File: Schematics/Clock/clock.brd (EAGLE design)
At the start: 53.3 x 50.3 mm, 13 parts, among them IC1 NE555N

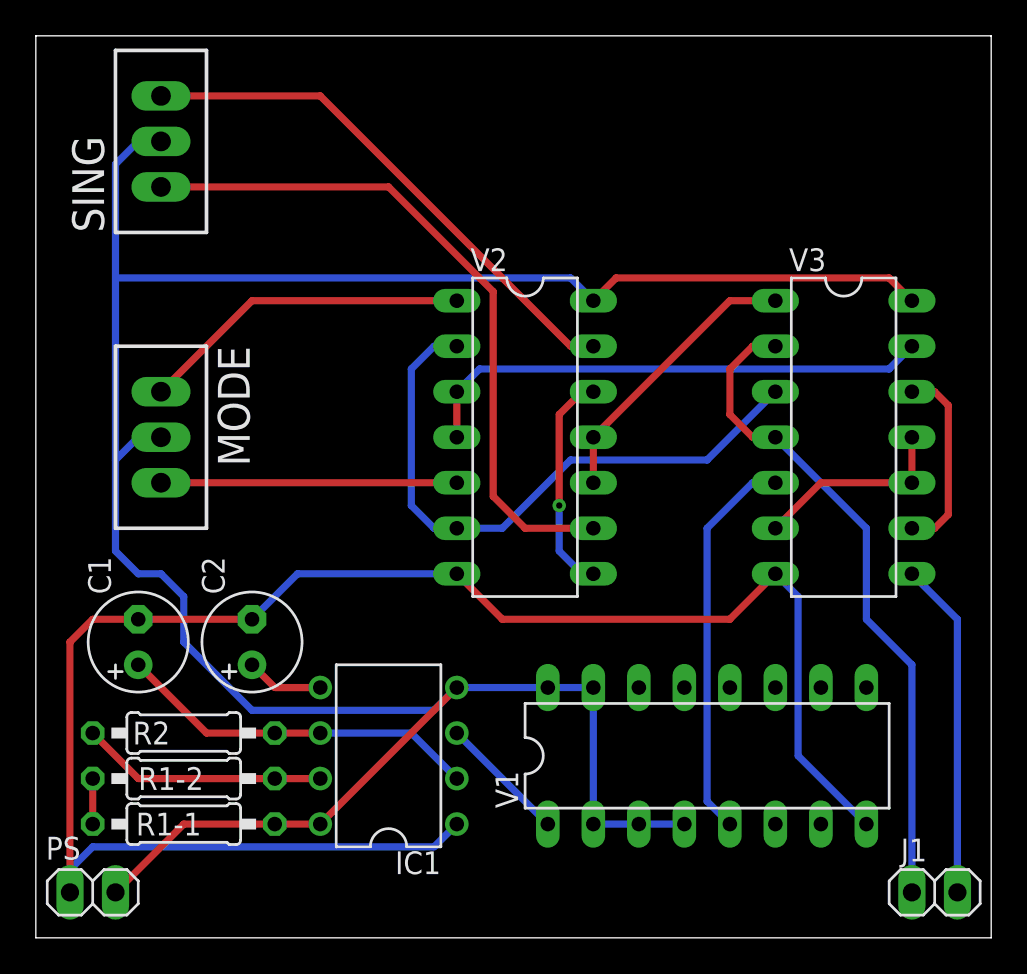
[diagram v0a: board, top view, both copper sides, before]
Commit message: Added pull down resisotors to NAND gates. Maybe 'single' will be button.
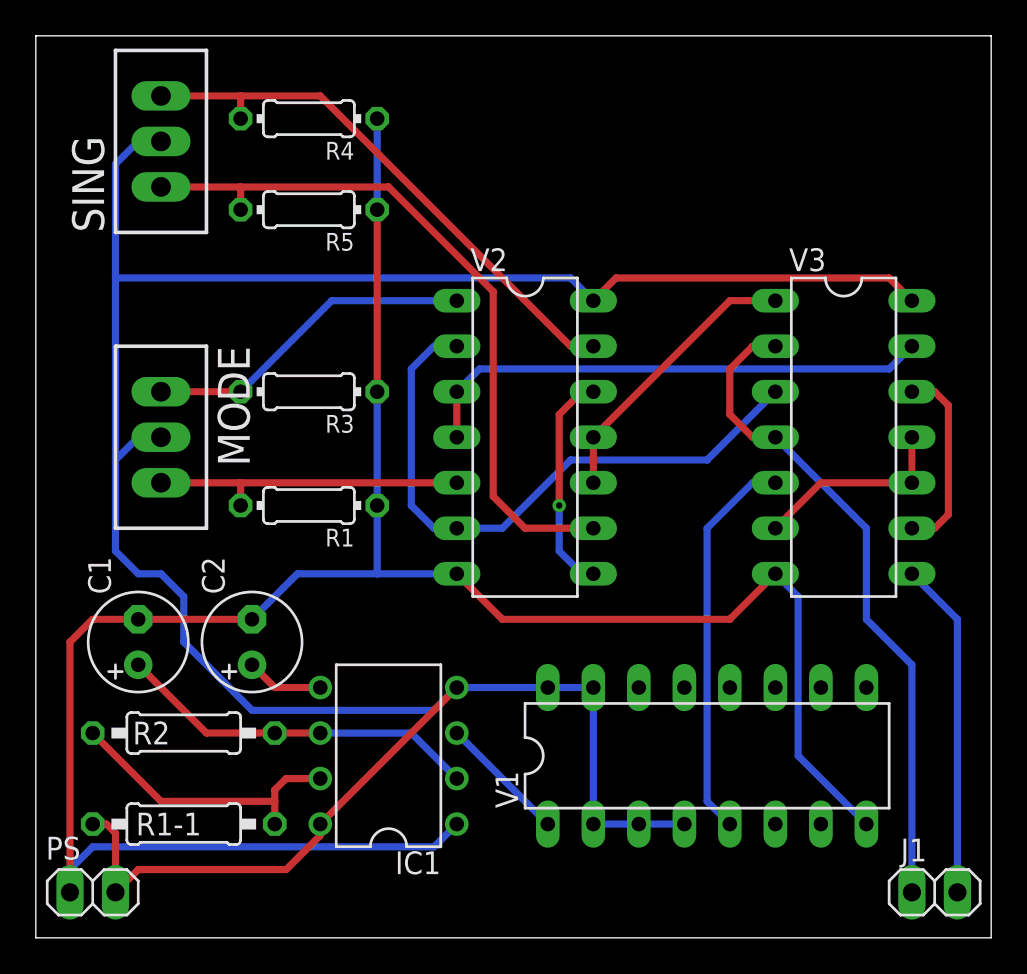
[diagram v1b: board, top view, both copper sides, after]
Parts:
- removed R1-2: (no value), rcl:0207/10
- added R1, R3, R4, R5: (no value), rcl:0204/7
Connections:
- removed net N$4: R1-1.1, R1-2.1
- net GND: now also R1.1, R3.1, R4.1, R5.1
- net N$11: now also R5.2
- net N$12: now also R4.2
- net N$2: now also R1-1.2; no longer R1-2.2
- net N$7: now also R3.2
- net N$8: now also R1.2
- net VCC: now also R1-1.1; no longer R1-1.2
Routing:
- net GND: track 97.0 -> 122.4 mm
- net VCC: track 142.6 -> 147.8 mm
- net N$2: track 13.8 -> 16.4 mm
- net N$4: track 2.54 -> 0.00 mm
- net N$12: track 29.9 -> 31.2 mm
- net N$8: track 16.5 -> 17.8 mm
- net N$11: track 38.7 -> 40.0 mm
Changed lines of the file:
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@@
 <attribute name="VALUE" x="5.9944" y="5.715" size="1.27" layer="27" ratio="10"/>
-</element>
-<element name="R1-2" library="rcl" library_urn="urn:adsk.eagle:library:334" package="0207/10" package3d_urn="urn:adsk.eagle:package:23491/2" value="" x="8.255" y="8.89" smashed="yes">
-<attribute name="NAME" x="5.715" y="8.255" size="1.27" layer="25" ratio="10"/>
-<attribute name="POPULARITY" value="81" x="40.005" y="-45.72" size="1.778" layer="27" display="off"/>
-<attribute name="SPICEPREFIX" value="R" x="40.005" y="-45.72" size="1.778" layer="27" display="off"/>
-<attribute name="VALUE" x="5.9944" y="8.255" size="1.27" layer="27" ratio="10"/>
 </element>
 <element name="R2" library="rcl" library_urn="urn:adsk.eagle:library:334" package="0207/10" package3d_urn="urn:adsk.eagle:package:23491/2" value="" x="8.255" y="11.43" smashed="yes" rot="R180">
@@
 <attribute name="POPULARITY" value="0" x="4.445" y="5.08" size="1.778" layer="27" rot="R270" display="off"/>
 <attribute name="VALUE" x="44.45" y="34.671" size="1.27" layer="27" ratio="10" rot="R270"/>
+</element>
+<element name="R1" library="rcl" library_urn="urn:adsk.eagle:library:334" package="0204/7" package3d_urn="urn:adsk.eagle:package:23498/2" value="" x="15.24" y="24.13" smashed="yes" rot="R180">
+<attribute name="NAME" x="17.78" y="22.8346" size="0.9906" layer="25" ratio="10" rot="R180"/>
+<attribute name="POPULARITY" value="79" x="15.24" y="24.13" size="1.778" layer="27" rot="R180" display="off"/>
+<attribute name="SPICEPREFIX" value="R" x="15.24" y="24.13" size="1.778" layer="27" rot="R180" display="off"/>
+<attribute name="VALUE" x="16.8656" y="24.6126" size="0.9906" layer="27" ratio="10" rot="R180"/>
+</element>
+<element name="R3" library="rcl" library_urn="urn:adsk.eagle:library:334" package="0204/7" package3d_urn="urn:adsk.eagle:package:23498/2" value="" x="15.24" y="30.48" smashed="yes" rot="R180">
+<attribute name="NAME" x="17.78" y="29.1846" size="0.9906" layer="25" ratio="10" rot="R180"/>
+<attribute name="POPULARITY" value="79" x="15.24" y="30.48" size="1.778" layer="27" rot="R180" display="off"/>
+<attribute name="SPICEPREFIX" value="R" x="15.24" y="30.48" size="1.778" layer="27" rot="R180" display="off"/>
+<attribute name="VALUE" x="16.8656" y="30.9626" size="0.9906" layer="27" ratio="10" rot="R180"/>
+</element>
+<element name="R4" library="rcl" library_urn="urn:adsk.eagle:library:334" package="0204/7" package3d_urn="urn:adsk.eagle:package:23498/2" value="" x="15.24" y="45.72" smashed="yes" rot="R180">
+<attribute name="NAME" x="17.78" y="44.4246" size="0.9906" layer="25" ratio="10" rot="R180"/>
+<attribute name="POPULARITY" value="79" x="15.24" y="45.72" size="1.778" layer="27" rot="R180" display="off"/>
+<attribute name="SPICEPREFIX" value="R" x="15.24" y="45.72" size="1.778" layer="27" rot="R180" display="off"/>
+<attribute name="VALUE" x="16.8656" y="46.2026" size="0.9906" layer="27" ratio="10" rot="R180"/>
+</element>
+<element name="R5" library="rcl" library_urn="urn:adsk.eagle:library:334" package="0204/7" package3d_urn="urn:adsk.eagle:package:23498/2" value="" x="15.24" y="40.64" smashed="yes" rot="R180">
+<attribute name="NAME" x="17.78" y="39.3446" size="0.9906" layer="25" ratio="10" rot="R180"/>
+<attribute name="POPULARITY" value="79" x="15.24" y="40.64" size="1.778" layer="27" rot="R180" display="off"/>
+<attribute name="SPICEPREFIX" value="R" x="15.24" y="40.64" size="1.778" layer="27" rot="R180" display="off"/>
+<attribute name="VALUE" x="16.8656" y="41.1226" size="0.9906" layer="27" ratio="10" rot="R180"/>
 </element>
 </elements>
@@
 <contactref element="R2" pad="2"/>
 <contactref element="IC1" pad="7"/>
-<contactref element="R1-2" pad="2"/>
-<wire x1="13.335" y1="8.89" x2="5.715" y2="8.89" width="0.4" layer="1"/>
-<wire x1="5.715" y1="8.89" x2="3.175" y2="11.43" width="0.4" layer="1"/>
-<wire x1="13.335" y1="8.89" x2="15.875" y2="8.89" width="0.4" layer="1"/>
+<contactref element="R1-1" pad="2"/>
+<wire x1="13.335" y1="6.35" x2="13.335" y2="7.62" width="0.4" layer="1"/>
+<wire x1="13.335" y1="7.62" x2="13.335" y2="8.255" width="0.4" layer="1"/>
+<wire x1="13.335" y1="8.255" x2="13.97" y2="8.89" width="0.4" layer="1"/>
+<wire x1="13.97" y1="8.89" x2="15.875" y2="8.89" width="0.4" layer="1"/>
+<wire x1="3.175" y1="11.43" x2="6.985" y2="7.62" width="0.4" layer="1"/>
+<wire x1="6.985" y1="7.62" x2="13.335" y2="7.62" width="0.4" layer="1"/>
 </signal>
 <signal name="N$3">
@@
 <contactref element="IC1" pad="8"/>
 <contactref element="IC1" pad="4"/>
-<contactref element="R1-1" pad="2"/>
 <contactref element="V1" pad="4"/>
 <contactref element="V1" pad="2"/>
@@
 <contactref element="V3" pad="14"/>
 <contactref element="V1" pad="16"/>
-<wire x1="13.335" y1="6.35" x2="15.875" y2="6.35" width="0.4" layer="1"/>
-<wire x1="4.445" y1="2.54" x2="8.255" y2="6.35" width="0.4" layer="1"/>
-<wire x1="8.255" y1="6.35" x2="13.335" y2="6.35" width="0.4" layer="1"/>
 <wire x1="15.875" y1="6.35" x2="23.495" y2="13.97" width="0.4" layer="1"/>
 <wire x1="31.115" y1="13.97" x2="31.115" y2="6.35" width="0.4" layer="16"/>
@@
 <wire x1="31.115" y1="35.56" x2="29.845" y2="36.83" width="0.4" layer="16"/>
 <wire x1="29.845" y1="36.83" x2="4.445" y2="36.83" width="0.4" layer="16"/>
+<contactref element="R1-1" pad="1"/>
+<wire x1="4.445" y1="2.54" x2="4.445" y2="5.842" width="0.4" layer="1"/>
+<wire x1="4.445" y1="5.842" x2="3.937" y2="6.35" width="0.4" layer="1"/>
+<wire x1="3.937" y1="6.35" x2="3.175" y2="6.35" width="0.4" layer="1"/>
+<wire x1="4.445" y1="2.54" x2="5.715" y2="3.81" width="0.4" layer="1"/>
+<wire x1="5.715" y1="3.81" x2="13.97" y2="3.81" width="0.4" layer="1"/>
+<wire x1="13.97" y1="3.81" x2="15.875" y2="5.715" width="0.4" layer="1"/>
+<wire x1="15.875" y1="5.715" x2="15.875" y2="6.35" width="0.4" layer="1"/>
 </signal>
 <signal name="GND">
@@
 <wire x1="42.545" y1="10.16" x2="42.545" y2="19.05" width="0.4" layer="16"/>
 <wire x1="12.065" y1="17.78" x2="14.605" y2="20.32" width="0.4" layer="16"/>
-<wire x1="14.605" y1="20.32" x2="23.495" y2="20.32" width="0.4" layer="16"/>
+<wire x1="14.605" y1="20.32" x2="19.05" y2="20.32" width="0.4" layer="16"/>
+<wire x1="19.05" y1="20.32" x2="23.495" y2="20.32" width="0.4" layer="16"/>
 <wire x1="41.275" y1="20.32" x2="38.735" y2="17.78" width="0.4" layer="1"/>
 <wire x1="26.035" y1="17.78" x2="23.495" y2="20.32" width="0.4" layer="1"/>
 <wire x1="38.735" y1="17.78" x2="26.035" y2="17.78" width="0.4" layer="1"/>
+<contactref element="R1" pad="1"/>
+<contactref element="R3" pad="1"/>
+<contactref element="R4" pad="1"/>
+<contactref element="R5" pad="1"/>
+<wire x1="19.05" y1="24.13" x2="19.05" y2="20.32" width="0.4" layer="16"/>
+<wire x1="19.05" y1="24.13" x2="19.05" y2="30.48" width="0.4" layer="16"/>
+<wire x1="19.05" y1="40.64" x2="19.05" y2="45.72" width="0.4" layer="16"/>
+<wire x1="19.05" y1="40.64" x2="19.05" y2="30.48" width="0.4" layer="1"/>
 </signal>
 <signal name="CLK-0">
@@
 <contactref element="V1" pad="1"/>
 <wire x1="23.495" y1="11.43" x2="28.575" y2="6.35" width="0.4" layer="16"/>
-</signal>
-<signal name="N$4">
-<contactref element="R1-2" pad="1"/>
-<contactref element="R1-1" pad="1"/>
-<wire x1="3.175" y1="6.35" x2="3.175" y2="8.89" width="0.4" layer="1"/>
 </signal>
 <signal name="CLK-1">
@@
 <contactref element="V2" pad="1"/>
 <contactref element="MODE" pad="1"/>
-<wire x1="6.985" y1="30.48" x2="12.065" y2="35.56" width="0.4" layer="1"/>
-<wire x1="12.065" y1="35.56" x2="23.495" y2="35.56" width="0.4" layer="1"/>
+<contactref element="R3" pad="2"/>
+<wire x1="6.985" y1="30.48" x2="11.43" y2="30.48" width="0.4" layer="1"/>
+<wire x1="11.43" y1="30.48" x2="16.51" y2="35.56" width="0.4" layer="16"/>
+<wire x1="16.51" y1="35.56" x2="23.495" y2="35.56" width="0.4" layer="16"/>
 </signal>
 <signal name="N$8">
 <contactref element="V2" pad="5"/>
 <contactref element="MODE" pad="3"/>
-<wire x1="6.985" y1="25.4" x2="23.495" y2="25.4" width="0.4" layer="1"/>
+<wire x1="6.985" y1="25.4" x2="11.43" y2="25.4" width="0.4" layer="1"/>
+<contactref element="R1" pad="2"/>
+<wire x1="11.43" y1="25.4" x2="23.495" y2="25.4" width="0.4" layer="1"/>
+<wire x1="11.43" y1="24.13" x2="11.43" y2="25.4" width="0.4" layer="1"/>
 </signal>
 <signal name="N$11">
 <contactref element="SING" pad="1"/>
 <contactref element="V2" pad="9"/>
-<wire x1="6.985" y1="41.91" x2="19.685" y2="41.91" width="0.4" layer="1"/>
+<wire x1="6.985" y1="41.91" x2="11.43" y2="41.91" width="0.4" layer="1"/>
+<wire x1="11.43" y1="41.91" x2="19.685" y2="41.91" width="0.4" layer="1"/>
 <wire x1="25.527" y1="24.638" x2="27.305" y2="22.86" width="0.4" layer="1"/>
 <wire x1="27.305" y1="22.86" x2="31.115" y2="22.86" width="0.4" layer="1"/>
 <wire x1="19.685" y1="41.91" x2="25.527" y2="36.068" width="0.4" layer="1"/>
 <wire x1="25.527" y1="36.068" x2="25.527" y2="24.638" width="0.4" layer="1"/>
+<contactref element="R5" pad="2"/>
+<wire x1="11.43" y1="40.64" x2="11.43" y2="41.91" width="0.4" layer="1"/>
 </signal>
 <signal name="N$12">
 <contactref element="SING" pad="3"/>
 <contactref element="V2" pad="13"/>
-<wire x1="6.985" y1="46.99" x2="15.875" y2="46.99" width="0.4" layer="1"/>
+<wire x1="6.985" y1="46.99" x2="11.43" y2="46.99" width="0.4" layer="1"/>
+<wire x1="11.43" y1="46.99" x2="15.875" y2="46.99" width="0.4" layer="1"/>
 <wire x1="29.845" y1="33.02" x2="31.115" y2="33.02" width="0.4" layer="1"/>
 <wire x1="15.875" y1="46.99" x2="29.845" y2="33.02" width="0.4" layer="1"/>
+<contactref element="R4" pad="2"/>
+<wire x1="11.43" y1="45.72" x2="11.43" y2="46.99" width="0.4" layer="1"/>
 </signal>
 <signal name="N$13">
